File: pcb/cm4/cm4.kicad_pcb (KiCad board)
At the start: 4 copper layers, 100 x 100 mm, 32 parts, among them J101 Conn_02x10_Row_Letter_First, J201 DF40C-100DS-0.4V_51_, J202 DF40C-100DS-0.4V_51_, J301 HR911130A, U201 SN74LV1T34DBV, U301 TPD4EUSB30, U302 TPD4EUSB30, U401 RT9742GGJ5

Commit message: update cm4 board
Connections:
- net /CM4-Board/ETH_GREEN renamed /CM4-Board/ETH_LED_G
- net /CM4-Board/ETH_YELLOW renamed /CM4-Board/ETH_LED_Y
- net /CM4-Board/TRD0+ renamed /CM4-Board/ETH_TRD0_P
- net /CM4-Board/TRD0- renamed /CM4-Board/ETH_TRD0_M
- net /CM4-Board/TRD1+ renamed /CM4-Board/ETH_TRD1_P
- net /CM4-Board/TRD1- renamed /CM4-Board/ETH_TRD1_M
- net /CM4-Board/TRD2+ renamed /CM4-Board/ETH_TRD2_P
- net /CM4-Board/TRD2- renamed /CM4-Board/ETH_TRD2_M
- net /CM4-Board/TRD3+ renamed /CM4-Board/ETH_TRD3_P
- net /CM4-Board/TRD3- renamed /CM4-Board/ETH_TRD3_M
- net /USB+ renamed /USB_DP
- net /USB- renamed /USB_DM
- net /USB_OTG_ID renamed /USB_ID

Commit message: update ALL parts
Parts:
- C101, C201: footprint Capacitor_Tantalum_SMD:CP_EIA-7343-43_Kemet-X_Pad2.25x2.55mm_HandSolder -> Capacitor_Tantalum_SMD:CP_EIA-7343-43_Kemet-X

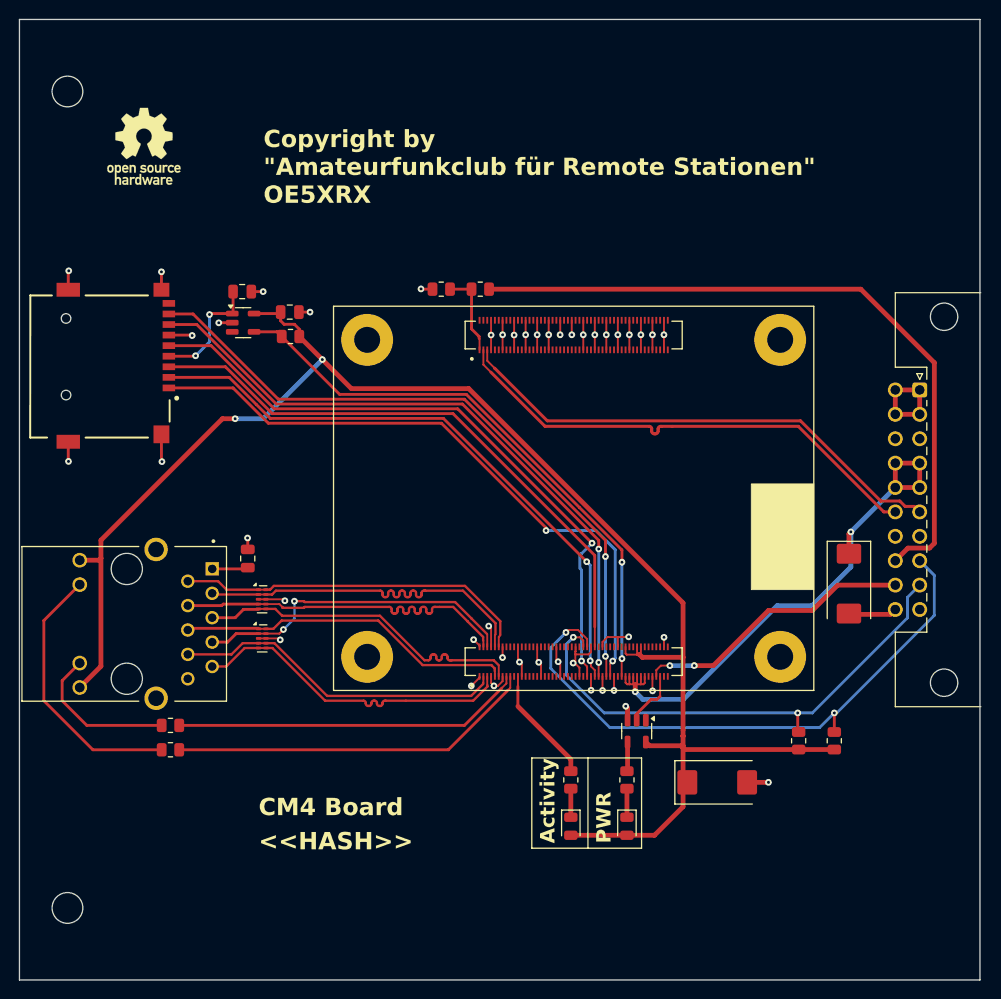
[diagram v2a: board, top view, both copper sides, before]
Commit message: rename differential nets correctly and fix cm4 footprint
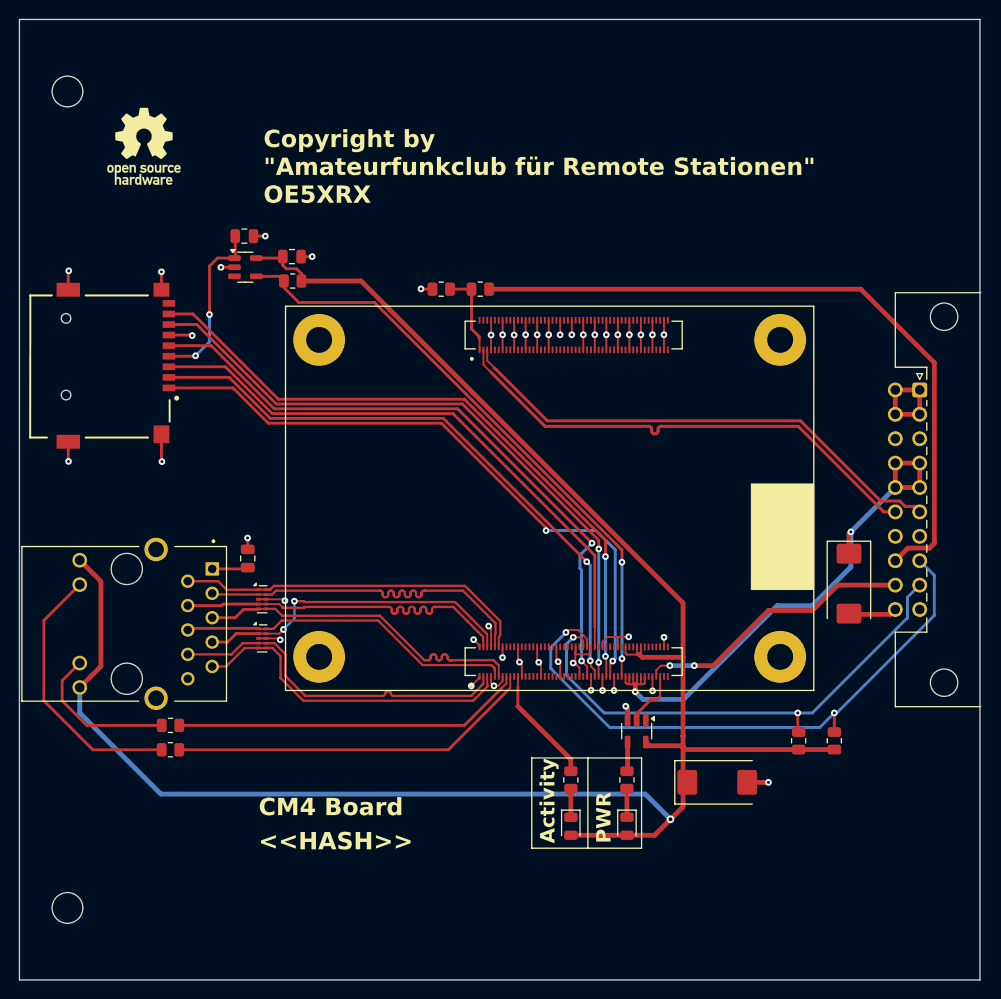
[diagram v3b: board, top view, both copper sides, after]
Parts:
- moved C402 5.78 mm to (116.6, 68.4)
- moved U401 5.78 mm to (116.7, 71.6)
- moved C401 5.78 mm to (121.6, 70.5)
- moved R401 5.78 mm to (121.7, 73.0)
- moved REF** 5.00 mm to (124.4, 112.2)
- moved REF** 5.00 mm to (124.4, 79.2)
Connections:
- net /CM4-Board/ETH_TRD0_M renamed /CM4-Board/ETH_TRD0_N
- net /CM4-Board/ETH_TRD1_M renamed /CM4-Board/ETH_TRD1_N
- net /CM4-Board/ETH_TRD2_M renamed /CM4-Board/ETH_TRD2_N
- net /CM4-Board/ETH_TRD3_M renamed /CM4-Board/ETH_TRD3_N
- net /USB_DM renamed /USB_D_N
- net /USB_DP renamed /USB_D_P
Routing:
- net +3V3: track 169.9 -> 206.5 mm, vias 2 -> 1
- net /MicroSD/SD_PWR: track 12.4 -> 18.0 mm
- net /CM4-Board/SD_PWR_ON: track 60.9 -> 63.4 mm
- net /CM4-Board/ETH_TRD3_P: track 34.8 -> 36.7 mm

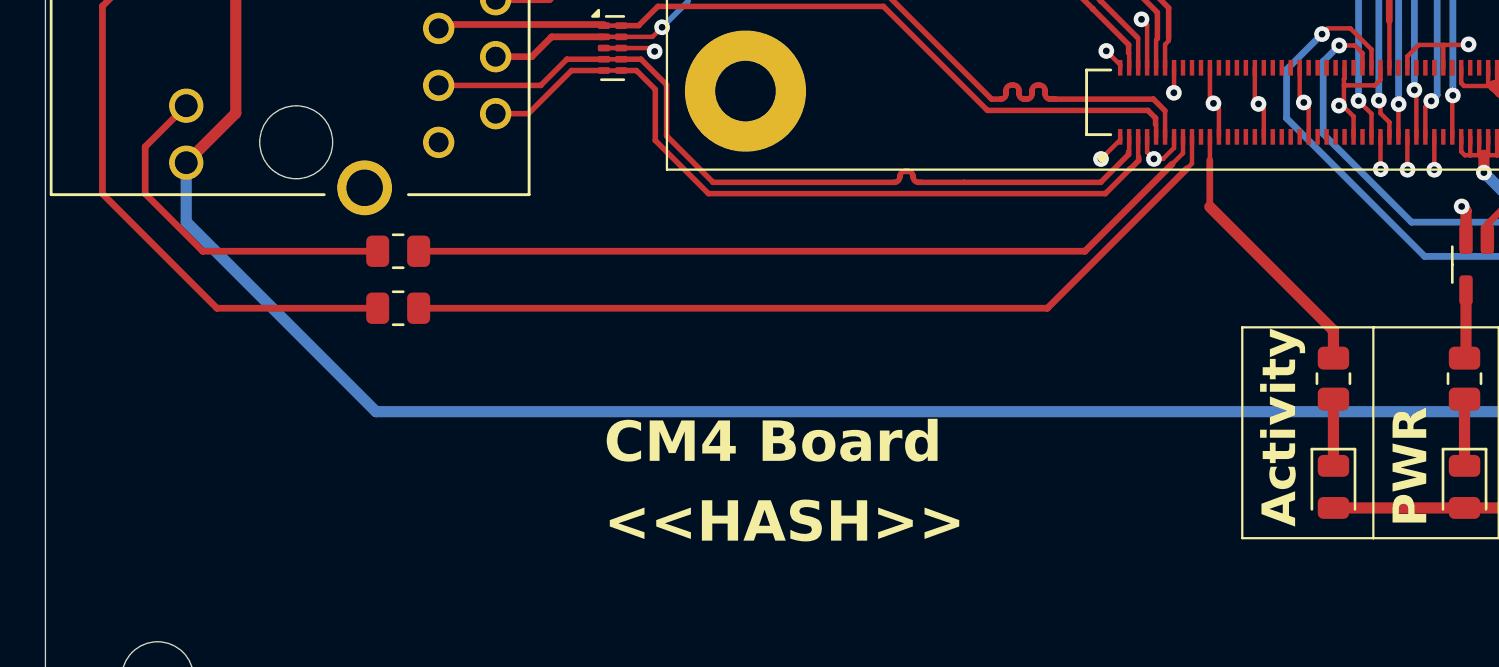
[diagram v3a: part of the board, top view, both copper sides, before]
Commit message: cm4: add debug uart
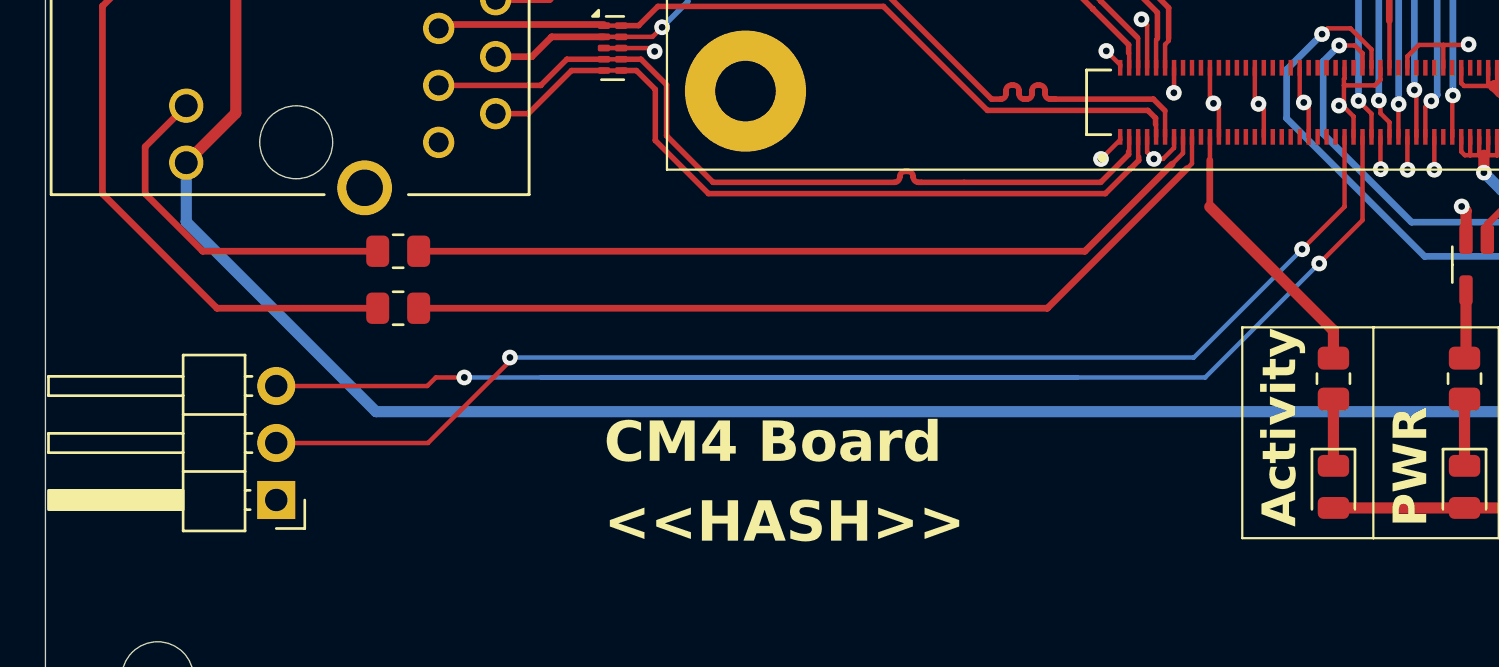
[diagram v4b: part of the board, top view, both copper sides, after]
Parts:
- added J102: Conn_01x03_Pin, Connector_PinHeader_2.54mm:PinHeader_1x03_P2.54mm_Horizontal, F.Cu at (103.5, 130.4)
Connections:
- J201 pad 51: unconnected-(J201-Pad51) -> /CM4-Board/RXD0
- J201 pad 55: unconnected-(J201-Pad55) -> /CM4-Board/TXD0
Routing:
- net /CM4-Board/TXD0: track 0.00 -> 102.9 mm, vias 0 -> 2
- net /CM4-Board/RXD0: track 0.00 -> 55.2 mm, vias 0 -> 2
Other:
- board text added: "GND"
- board text added: "RX"
- board text added: "TX"
